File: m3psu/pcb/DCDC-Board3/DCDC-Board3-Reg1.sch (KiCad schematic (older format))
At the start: 38 parts

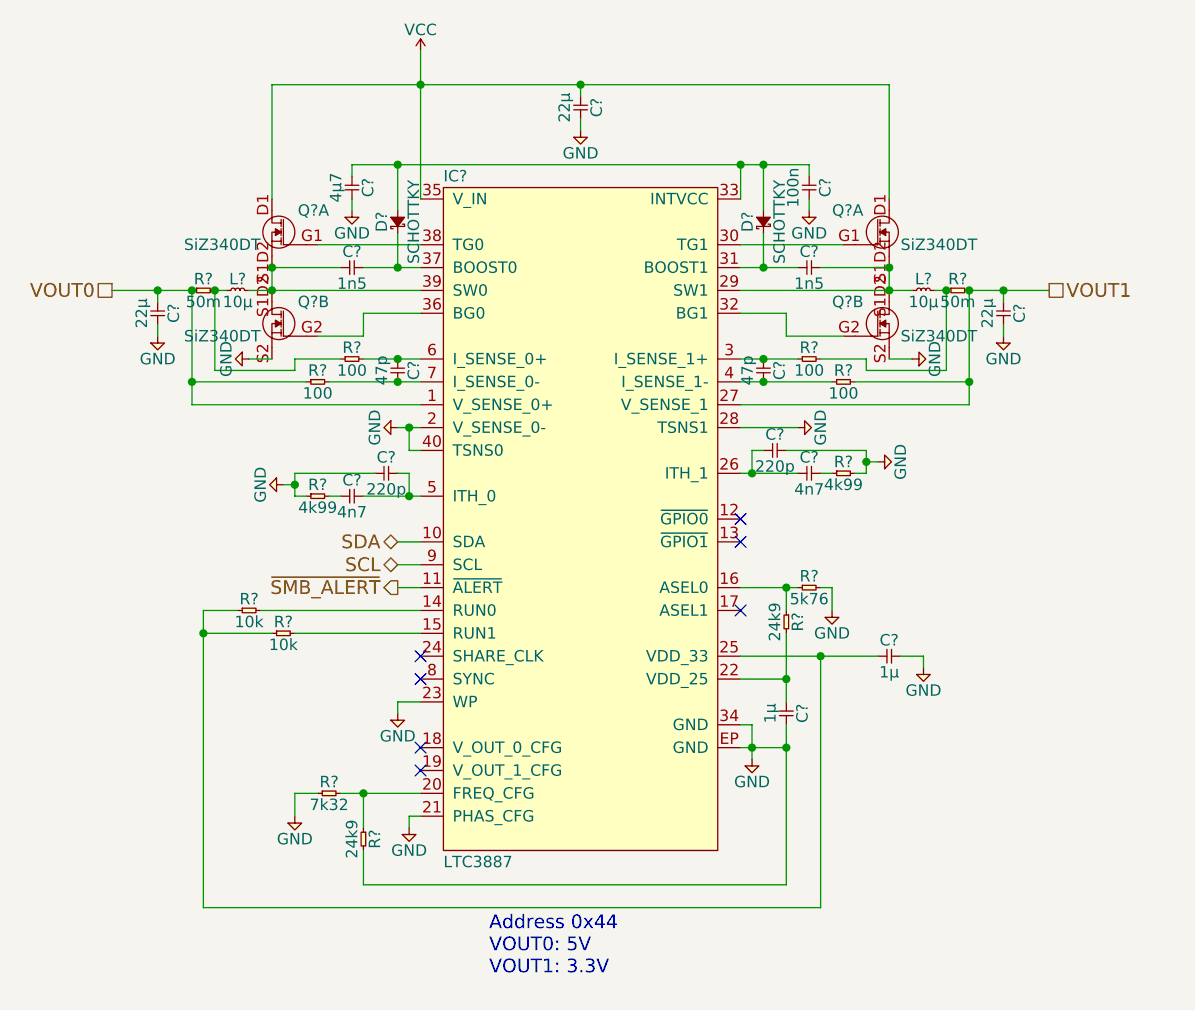
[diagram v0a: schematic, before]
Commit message: create DCDC1/2/3 from prototype
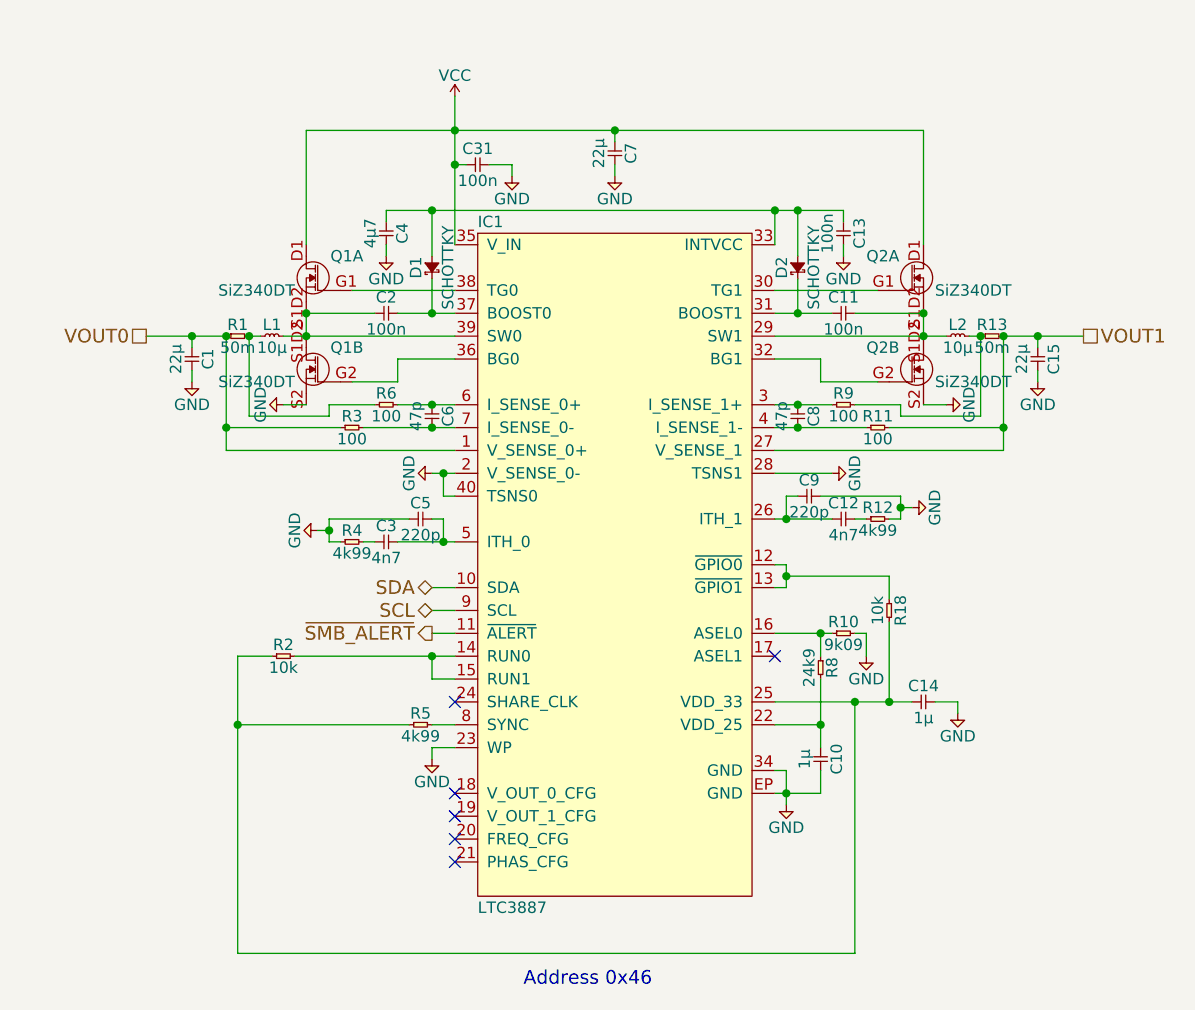
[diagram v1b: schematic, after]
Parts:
- removed C? (x2): 1n5, agg:0402, symbol C
- removed C?: 4µ7, agg:0603, symbol C
- removed C? (x3): 22µ, agg:0805, symbol C
- removed C? (x2): 47p, agg:0402, symbol C
- removed C? (x2): 1µ, agg:0402, symbol C
- removed C?: 100n, agg:0402, symbol C
- removed C? (x2): 4n7, agg:0402, symbol C
- removed C? (x2): 220p, agg:0402, symbol C
- removed D? (x2): SCHOTTKY, agg:0603-LED, symbol SCHOTTKY
- removed IC?: LTC3887, agg:QFN-40-EP-LTC-UJ, symbol LTC3887
- removed L? (x2): 10µ, agg:TYS5040, symbol L
- removed Q? (x4): SiZ340DT, agg:PowerPair3x3, symbol SiZ340DT
- removed R? (x2): 50m, agg:0603, symbol R
- removed R? (x4): 100, agg:0402, symbol R
- removed R?: 5k76, agg:0402, symbol R
- removed R? (x2): 24k9, agg:0402, symbol R
- removed R? (x2): 4k99, agg:0402, symbol R
- removed R?: 7k32, agg:0402, symbol R
- removed R? (x2): 10k, agg:0402, symbol R
- added C1, C15, C7: 22µ, agg:0805, symbol C
- added C10, C14: 1µ, agg:0402, symbol C
- added C11, C13, C2, C31: 100n, agg:0402, symbol C
- added C12, C3: 4n7, agg:0402, symbol C
- added C4: 4µ7, agg:0402, symbol C
- added C5, C9: 220p, agg:0402, symbol C
- added C6, C8: 47p, agg:0402, symbol C
- added D1, D2: SCHOTTKY, agg:0603-LED, symbol SCHOTTKY
- added IC1: LTC3887, agg:QFN-40-EP-LTC-UJ, symbol LTC3887
- added L1, L2: 10µ, agg:TYS5040, symbol L
- added Q1, Q2: SiZ340DT, agg:PowerPair3x3, symbol SiZ340DT
- added R1, R13: 50m, agg:0603, symbol R
- added R10: 9k09, agg:0402, symbol R
- added R11, R3, R6, R9: 100, agg:0402, symbol R
- added R12, R4, R5: 4k99, agg:0402, symbol R
- added R18, R2: 10k, agg:0402, symbol R
- added R8: 24k9, agg:0402, symbol R
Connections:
- net GND: now also C1.2, C10.2, C13.2, C14.2, C15.2, C31.2, C4.2, C5.1, C7.2, C9.2, IC1.2 (V_SENSE_0-), IC1.23 (WP), IC1.28 (TSNS1), IC1.34 (GND), IC1.40 (TSNS0), IC1.EP (GND), Q1.S2, Q2.S2, R10.2, R12.2, R4.1
- net SCL: now also IC1.9 (SCL)
- net SDA: now also IC1.10 (SDA)
- net VCC: now also C31.1, C7.1, IC1.35 (V_IN), Q1.D1 (S1D2), Q2.D1 (S1D2)
- net VOUT0: now also C1.1, IC1.1 (V_SENSE_0+), R1.1, R3.1
- net VOUT1: now also C15.1, IC1.27 (V_SENSE_1), R11.2, R13.2
- net ~SMB_ALERT: now also IC1.11 (~ALERT)
- new net: IC1.12 (~GPIO0), IC1.13 (~GPIO1), R18.1
- new net: IC1.14 (RUN0), IC1.15 (RUN1), R2.2
- new net: IC1.16 (ASEL0), R10.1, R8.1
- new net: C10.1, IC1.22 (VDD_25), R8.2
- new net: C14.1, IC1.25 (VDD_33), R18.2, R2.1, R5.1
- new net: C12.1, C9.1, IC1.26 (ITH_1)
- new net: C11.2, IC1.29 (SW1), L2.1, Q2.S1D2, Q2.S1D2
- new net: C8.1, IC1.3 (I_SENSE_1+), R9.1
- new net: IC1.30 (TG1), Q2.G1
- new net: C11.1, D2.1, IC1.31 (BOOST1)
- new net: IC1.32 (BG1), Q2.G2
- new net: C13.1, C4.1, D1.2, D2.2, IC1.33 (INTVCC)
- new net: IC1.36 (BG0), Q1.G2
- new net: C2.2, D1.1, IC1.37 (BOOST0)
- new net: IC1.38 (TG0), Q1.G1
- new net: C2.1, IC1.39 (SW0), L1.2, Q1.S1D2, Q1.S1D2
- new net: C8.2, IC1.4 (I_SENSE_1-), R11.1
- new net: C3.2, C5.2, IC1.5 (ITH_0)
- new net: C6.1, IC1.6 (I_SENSE_0+), R6.2
- new net: C6.2, IC1.7 (I_SENSE_0-), R3.2
- new net: IC1.8 (SYNC), R5.2
- new net: L2.2, R13.1, R9.2
- new net: L1.1, R1.2, R6.1
- new net: C12.2, R12.1
- new net: C3.1, R4.2
- no-connect marks 7 -> 6
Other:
- note added: "Address 0x46"
- note removed: "Address 0x44\nVOUT0: 5V\nVOUT1: 3.3V"
